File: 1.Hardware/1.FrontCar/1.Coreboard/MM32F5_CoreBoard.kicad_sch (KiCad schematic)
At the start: 68 parts, among them J1 IPS114, J2 USB-Type-C, J3 BTB_02x30, J4 BTB_02x30, J5 SH1.0_4P, J6 SH1.0_2P, J7 SH1.0_2P, SW1 3x4, SW2 3x4, SW3 3x4, SW4 3x4, U2 RT9013-33GB, U3 CH343P, U4 SN65HVD232, U5 SN65HVD232, U6 MM32F5277E9P, U7 MPU-6050, Y1 32.768KHz, Y2 8MHz

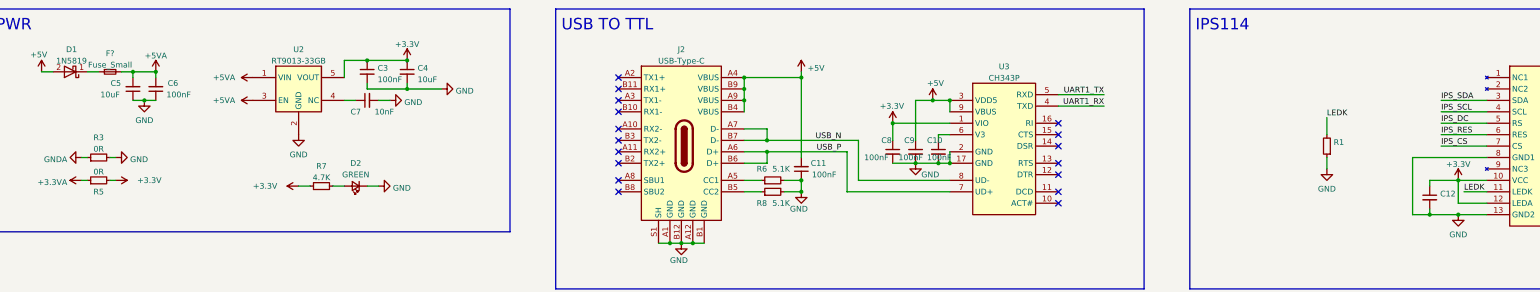
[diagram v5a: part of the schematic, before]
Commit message: 增加保险丝
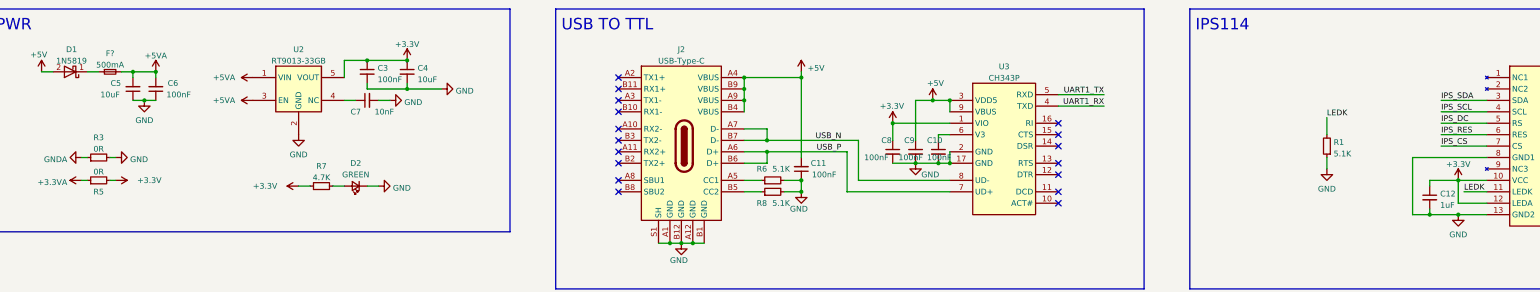
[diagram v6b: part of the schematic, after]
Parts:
- C12: value (none) -> 1uF
- F?: value Fuse_Small -> 500mA; footprint (none) -> Fuse:Fuse_0603_1608Metric
- R1: value (none) -> 5.1K
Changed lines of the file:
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@@
       (effects (font (size 1.27 1.27)) (justify left))
     )
-    (property "Value" "" (id 1) (at 342.6841 60.1285 0)
+    (property "Value" "1uF" (id 1) (at 342.6841 60.1285 0)
       (effects (font (size 1.27 1.27)) (justify left))
     )
@@
     (in_bom yes) (on_board yes) (fields_autoplaced)
     (property "Reference" "F?" (id 0) (at 46.99 26.3992 0))
-    (property "Value" "Fuse_Small" (id 1) (at 46.99 28.9361 0))
-    (property "Footprint" "" (id 2) (at 46.99 30.48 0)
+    (property "Value" "500mA" (id 1) (at 46.99 28.9361 0))
+    (property "Footprint" "Fuse:Fuse_0603_1608Metric" (id 2) (at 46.99 30.48 0)
       (effects (font (size 1.27 1.27)) hide)
     )
@@
       (effects (font (size 1.27 1.27)) (justify right))
     )
-    (property "Value" "" (id 1) (at 318.9986 48.6922 0)
+    (property "Value" "5.1K" (id 1) (at 318.9986 48.6922 0)
       (effects (font (size 1.27 1.27)) (justify right))
     )
@@
     )
     (path "/87123f42-2faf-4173-93eb-3d1b5761833c"
-      (reference "F?") (unit 1) (value "Fuse_Small") (footprint "")
+      (reference "F?") (unit 1) (value "500mA") (footprint "Fuse:Fuse_0603_1608Metric")
     )
     (path "/dc48cb12-ea35-4f7d-a2e1-838d59de09d2"

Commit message: 核心板原理图完成
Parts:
- removed Y2: 8MHz, ErBW_s:Crystal_SMD_3213_3P, symbol Device:Crystal_GND2_Small
- added Y2: 8MHz, ErBW_s:Crystal_SMD_3225_4P, symbol Device:Crystal_GND24_Small
- gave numbers to parts that had none: 1
- renumbered C3 to C1, C12 to C10, C14 to C11, C15 to C12, C16 to C13, C17 to C14, C18 to C15, C19 to C16, C20 to C17, C21 to C18, C22 to C19, C4 to C2, C23 to C20, C24 to C21, C25 to C22, C26 to C23, C27 to C24, C28 to C25, C29 to C26, C30 to C27, C31 to C28, C32 to C29, C5 to C3, C33 to C30, C34 to C31, C6 to C4, C7 to C5, C8 to C6, C9 to C7, C10 to C8, C11 to C9, R12 to R10, R13 to R11, R14 to R12, R15 to R13, R16 to R14, R17 to R15, R3 to R2, R5 to R3, R6 to R4, R7 to R5, R8 to R6, R9 to R7, R10 to R8, R11 to R9, U2 to U1, U3 to U2, U4 to U3, U5 to U4, U6 to U5, U7 to U6
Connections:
- net +5VA: now also J3.47 (Pin_47), J3.49 (Pin_49), J3.51 (Pin_51), J3.53 (Pin_53), J3.55 (Pin_55), J3.57 (Pin_57), J3.59 (Pin_59)
- net 1DIR: now also J3.21 (Pin_21), J4.20 (Pin_20)
- net 1LSB: now also J3.20 (Pin_20)
- net 1PWM: now also J4.18 (Pin_18)
- net 2DIR: now also J4.16 (Pin_16), J4.52 (Pin_52)
- net 2LSB: now also J4.49 (Pin_49)
- net 2PWM: now also J4.14 (Pin_14)
- net ADC_DIS: now also J4.22 (Pin_22)
- net ADC_VBAT: now also J4.24 (Pin_24)
- net CAM_D0: now also J4.6 (Pin_6)
- net CAM_D1: now also J4.5 (Pin_5)
- net CAM_D2: now also J4.8 (Pin_8)
- net CAM_D3: now also J4.7 (Pin_7)
- net CAM_D4: now also J4.10 (Pin_10)
- net CAM_D5: now also J4.9 (Pin_9)
- net CAM_D6: now also J4.12 (Pin_12)
- net CAM_D7: now also J4.11 (Pin_11)
- net CAM_PLCK: now also J4.2 (Pin_2)
- net CAM_RXD: now also J4.4 (Pin_4), U5.116 (PD2); no longer U5.113 (PC12)
- net CAM_TXD: now also J4.1 (Pin_1), U5.113 (PC12); no longer U5.116 (PD2)
- net CAM_VSYNC: now also J4.3 (Pin_3)
- net CAN1_H: now also J3.22 (Pin_22)
- net CAN1_L: now also J3.24 (Pin_24)
- net CAN2_H: now also J4.40 (Pin_40)
- net CAN2_L: now also J4.38 (Pin_38)
- net ELEMAG1: now also J4.13 (Pin_13)
- net ELEMAG2: now also J4.15 (Pin_15)
- net ELEMAG3: now also J4.17 (Pin_17)
- net ELEMAG4: now also J4.19 (Pin_19)
- net ELEMAG5: now also J4.21 (Pin_21)
- net ENCODER_A: now also J4.53 (Pin_53)
- net ENCODER_B: now also J4.56 (Pin_56)
- net GND: now also J3.46 (Pin_46), J3.48 (Pin_48), J3.50 (Pin_50), J3.52 (Pin_52), J3.54 (Pin_54), J3.56 (Pin_56), J3.58 (Pin_58), J3.60 (Pin_60), Y2.2, Y2.4
- net KEY_CENTER: now also J4.54 (Pin_54)
- net MAPLE_CLK: now also J4.35 (Pin_35)
- net MAPLE_CS: now also J4.36 (Pin_36)
- net MAPLE_MISO: now also J4.37 (Pin_37)
- net MAPLE_MOSI: now also J4.39 (Pin_39)
- net OSC_IN: now also Y2.3
- net PA10: now also J4.59 (Pin_59)
- net PA8: now also J4.57 (Pin_57)
- net PA9: now also J4.60 (Pin_60)
- net PB0: now also J4.26 (Pin_26)
- net PB1: now also J4.25 (Pin_25)
- net PB10: now also J4.41 (Pin_41)
- net PB11: now also J4.44 (Pin_44)
- net PB14: now also J4.43 (Pin_43)
- net PB15: now also J4.46 (Pin_46)
- net PB2-BOOT1: now also J4.28 (Pin_28)
- net PB3: now also J3.19 (Pin_19)
- net PC10: now also J3.8 (Pin_8)
- net PC11: now also J3.7 (Pin_7)
- net PC13: now also J3.31 (Pin_31)
- net PC5: now also J4.23 (Pin_23)
- net PC8: now also J4.55 (Pin_55)
- net PC9: now also J4.58 (Pin_58)
- net PD0: now also J3.9 (Pin_9)
- net PD1: now also J3.10 (Pin_10)
- net PD10: now also J4.47 (Pin_47)
- net PD11: now also J4.50 (Pin_50)
- net PD15: now also J4.51 (Pin_51)
- net PD3: now also J3.11 (Pin_11)
- net PD8: now also J4.45 (Pin_45)
- net PD9: now also J4.48 (Pin_48)
- net PE0: now also J3.23 (Pin_23)
- net PE1: now also J3.26 (Pin_26)
- net PE10: now also J4.33 (Pin_33)
- net PE15: now also J4.42 (Pin_42)
- net PE2: now also J3.25 (Pin_25)
- net PE3: now also J3.27 (Pin_27)
- net PE4: now also J3.28 (Pin_28)
- net PE9: now also J4.34 (Pin_34)
- net PF0: now also J3.32 (Pin_32)
- net PF1: now also J3.33 (Pin_33)
- net PF10: now also J3.42 (Pin_42)
- net PF11: now also J4.27 (Pin_27)
- net PF12: now also J4.30 (Pin_30)
- net PF13: now also J4.29 (Pin_29)
- net PF14: now also J4.32 (Pin_32)
- net PF15: now also J4.31 (Pin_31)
- net PF2: now also J3.34 (Pin_34)
- net PF3: now also J3.35 (Pin_35)
- net PF4: now also J3.36 (Pin_36)
- net PF5: now also J3.37 (Pin_37)
- net PF6: now also J3.38 (Pin_38)
- net PF7: now also J3.39 (Pin_39)
- net PF8: now also J3.40 (Pin_40)
- net PF9: now also J3.41 (Pin_41)
- net PG10: now also J3.13 (Pin_13)
- net PG11: now also J3.14 (Pin_14)
- net PG12: now also J3.15 (Pin_15)
- net PG13: now also J3.16 (Pin_16)
- net PG14: now also J3.17 (Pin_17)
- net PG15: now also J3.18 (Pin_18)
- net PG9: now also J3.12 (Pin_12)
- net PH2: now also J3.6 (Pin_6)
- net RST: now also J3.45 (Pin_45)
- net SERVO: now also J3.5 (Pin_5)
- net SWCLK: now also J3.1 (Pin_1)
- net SWDIO: now also J3.2 (Pin_2)
- net TOF_SCL: now also J3.29 (Pin_29)
- net TOF_SDA: now also J3.30 (Pin_30)
- net UART1_RX: now also J3.4 (Pin_4)
- net UART1_TX: now also J3.3 (Pin_3)
- net AUX_SCL: now reaches J3.43 (Pin_43)
- net AUX_SCL: now also U6.7 (AUX_SCL)
- net AUX_SDA: now reaches J3.44 (Pin_44)
- net AUX_SDA: now also U6.6 (AUX_SDA)
- net at C25.1, R13.2: now also Y2.1
- no-connect marks 20 -> 18
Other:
- moved on the sheet: J4

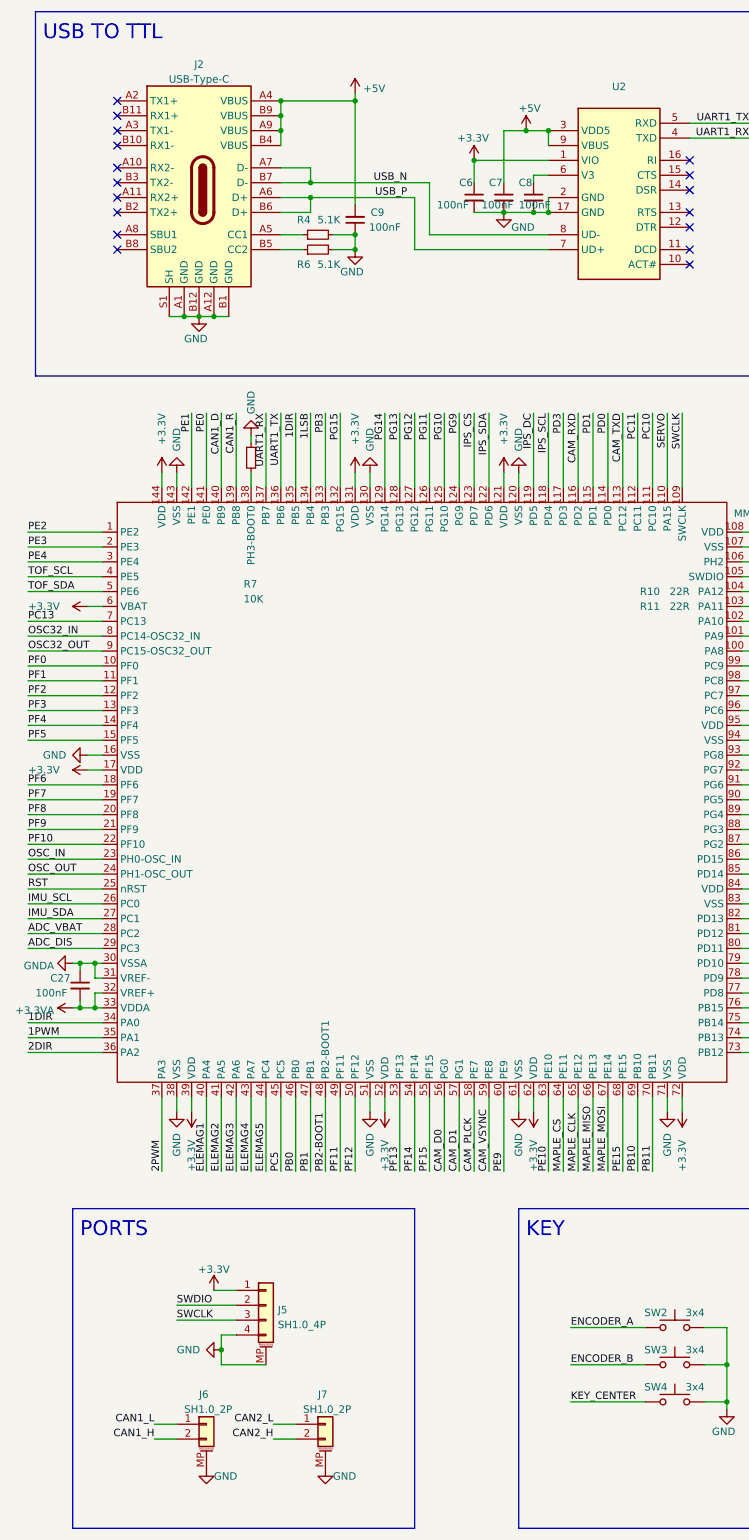
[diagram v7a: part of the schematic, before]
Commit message: 初步绘制核心板pcb
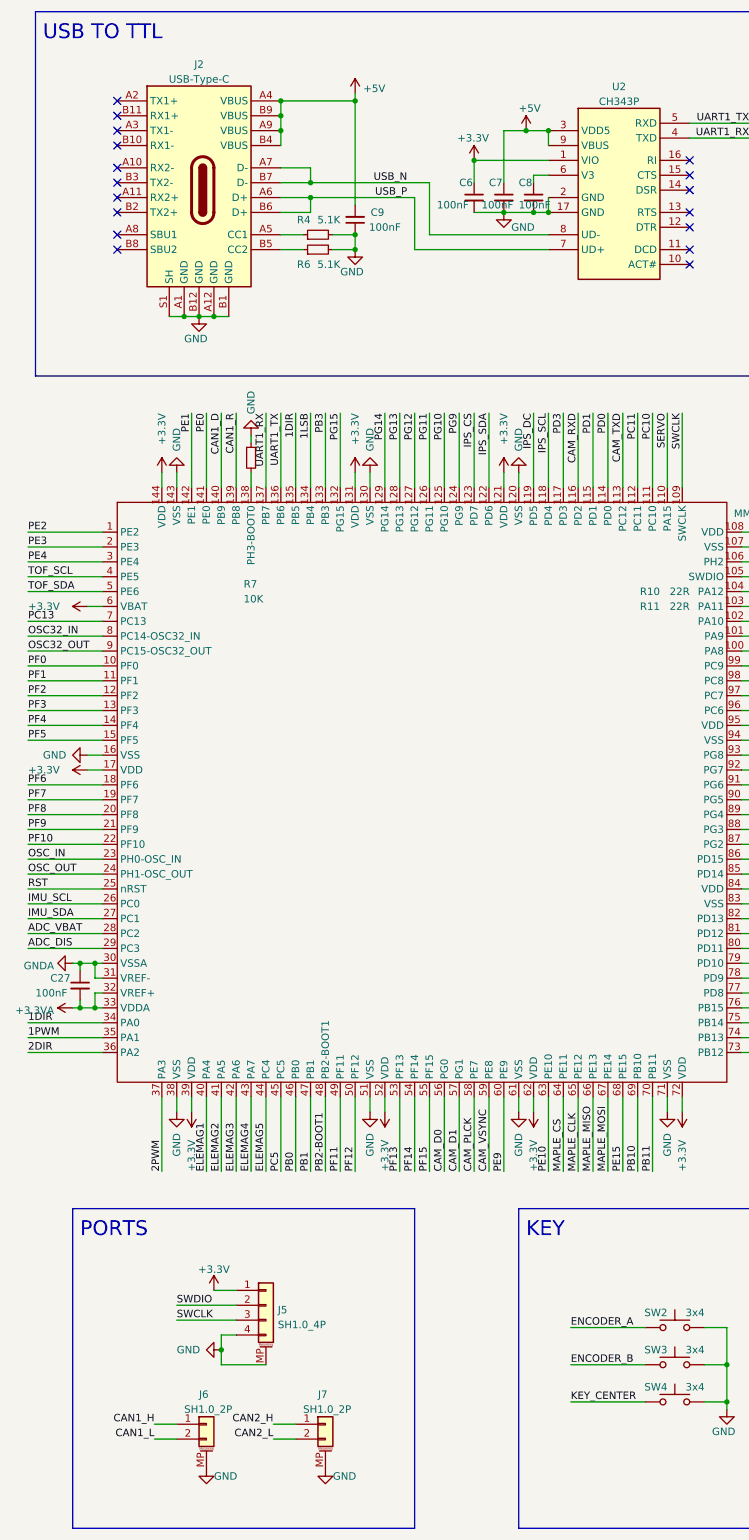
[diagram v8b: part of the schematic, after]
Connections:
- net CAN1_H: now also J6.1 (Pin_1); no longer J6.2 (Pin_2)
- net CAN1_L: now also J6.2 (Pin_2); no longer J6.1 (Pin_1)
- net CAN2_H: now also J7.1 (Pin_1); no longer J7.2 (Pin_2)
- net CAN2_L: now also J7.2 (Pin_2); no longer J7.1 (Pin_1)
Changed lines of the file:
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@@
   (no_connect (at 160.02 48.26))
   (no_connect (at 257.81 44.45))
-  (wire (pts (xy 190.5 260.35) (xy 186.69 260.35))
-    (stroke (width 0) (type default) (color 0 0 0 0))
-  )
   (wire (pts (xy 336.55 172.72) (xy 323.85 172.72))
     (stroke (width 0) (type default) (color 0 0 0 0))
@@
     (stroke (width 0) (type default) (color 0 0 0 0))
   )
+  (wire (pts (xy 190.5 260.35) (xy 186.69 260.35))
+    (stroke (width 0) (type default) (color 0 0 0 0))
+  )
   (wire (pts (xy 298.45 200.66) (xy 311.15 200.66))
     (stroke (width 0) (type default) (color 0 0 0 0))
@@
     (stroke (width 0) (type default) (color 0 0 0 0))
   )
+  (wire (pts (xy 170.18 257.81) (xy 166.37 257.81))
+    (stroke (width 0) (type default) (color 0 0 0 0))
+  )
   (polyline (pts (xy 287.02 78.74) (xy 398.78 78.74))
     (stroke (width 0) (type default) (color 0 0 0 0))
@@
     (stroke (width 0) (type default) (color 0 0 0 0))
   )
+  (wire (pts (xy 170.18 260.35) (xy 166.37 260.35))
+    (stroke (width 0) (type default) (color 0 0 0 0))
+  )
   (wire (pts (xy 104.14 251.46) (xy 101.6 251.46))
     (stroke (width 0) (type default) (color 0 0 0 0))
@@
     (stroke (width 0) (type default) (color 0 0 0 0))
   )
-  (wire (pts (xy 190.5 257.81) (xy 186.69 257.81))
-    (stroke (width 0) (type default) (color 0 0 0 0))
-  )
   (wire (pts (xy 298.45 170.18) (xy 311.15 170.18))
     (stroke (width 0) (type default) (color 0 0 0 0))
@@
     (stroke (width 0) (type default) (color 0 0 0 0))
   )
-  (wire (pts (xy 170.18 257.81) (xy 166.37 257.81))
-    (stroke (width 0) (type default) (color 0 0 0 0))
-  )
   (wire (pts (xy 387.35 215.9) (xy 374.65 215.9))
     (stroke (width 0) (type default) (color 0 0 0 0))
@@
     (stroke (width 0) (type default) (color 0 0 0 0))
   )
+  (wire (pts (xy 190.5 257.81) (xy 186.69 257.81))
+    (stroke (width 0) (type default) (color 0 0 0 0))
+  )
   (wire (pts (xy 269.24 168.91) (xy 266.7 168.91))
     (stroke (width 0) (type default) (color 0 0 0 0))
@@
     (stroke (width 0) (type default) (color 0 0 0 0))
   )
-  (wire (pts (xy 170.18 260.35) (xy 166.37 260.35))
-    (stroke (width 0) (type default) (color 0 0 0 0))
-  )
   (wire (pts (xy 257.81 35.56) (xy 267.97 35.56))
     (stroke (width 0) (type default) (color 0 0 0 0))
@@
     (effects (font (size 1.27 1.27)) (justify left bottom))
   )
+  (label "CAN2_H" (at 186.69 257.81 180)
+    (effects (font (size 1.27 1.27)) (justify right bottom))
+  )
   (label "PF5" (at 144.78 140.97 0)
     (effects (font (size 1.27 1.27)) (justify left bottom))
@@
     (effects (font (size 1.27 1.27)) (justify left bottom))
   )
-  (label "CAN2_H" (at 186.69 260.35 180)
+  (label "PC8" (at 387.35 165.1 180)
     (effects (font (size 1.27 1.27)) (justify right bottom))
   )
-  (label "PC8" (at 387.35 165.1 180)
+  (label "CAN1_L" (at 166.37 260.35 180)
     (effects (font (size 1.27 1.27)) (justify right bottom))
   )
@@
     (effects (font (size 1.27 1.27)) (justify left bottom))
   )
+  (label "CAN2_L" (at 186.69 260.35 180)
+    (effects (font (size 1.27 1.27)) (justify right bottom))
+  )
   (label "CAN2_L" (at 386.08 118.11 0)
     (effects (font (size 1.27 1.27)) (justify left bottom))
@@
     (effects (font (size 1.27 1.27)) (justify left bottom))
   )
-  (label "CAN1_H" (at 166.37 260.35 180)
-    (effects (font (size 1.27 1.27)) (justify right bottom))
-  )
   (label "ELEMAG4" (at 387.35 210.82 180)
     (effects (font (size 1.27 1.27)) (justify right bottom))
@@
     (effects (font (size 1.27 1.27)) (justify left bottom))
   )
+  (label "CAN1_H" (at 166.37 257.81 180)
+    (effects (font (size 1.27 1.27)) (justify right bottom))
+  )
   (label "PD1" (at 336.55 170.18 180)
     (effects (font (size 1.27 1.27)) (justify right bottom))
@@
     (effects (font (size 1.27 1.27)) (justify left bottom))
   )
-  (label "CAN1_L" (at 166.37 257.81 180)
-    (effects (font (size 1.27 1.27)) (justify right bottom))
-  )
   (label "PD1" (at 241.3 85.09 270)
     (effects (font (size 1.27 1.27)) (justify right bottom))
@@
     (effects (font (size 1.27 1.27)) (justify left bottom))
   )
-  (label "CAN2_L" (at 186.69 257.81 180)
-    (effects (font (size 1.27 1.27)) (justify right bottom))
-  )
   (label "PC8" (at 279.4 130.81 180)
     (effects (font (size 1.27 1.27)) (justify right bottom))
@@
     (in_bom yes) (on_board yes) (fields_autoplaced)
     (property "Reference" "U2" (id 0) (at 245.745 29.3202 0))
-    (property "Value" "" (id 1) (at 245.745 31.8571 0))
-    (property "Footprint" "" (id 2) (at 245.11 66.04 0)
+    (property "Value" "CH343P" (id 1) (at 245.745 31.8571 0))
+    (property "Footprint" "Package_DFN_QFN:QFN-16-1EP_3x3mm_P0.5mm_EP1.7x1.7mm" (id 2) (at 245.11 66.04 0)
       (effects (font (size 1.27 1.27)) hide)
     )
